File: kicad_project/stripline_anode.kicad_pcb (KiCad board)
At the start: 6 copper layers, 240 x 333.1 mm, 31 parts, among them J1 QRM8-078-05.0-L-D-A, U1 anode_pad, U10 anode_pad, U11 anode_pad, U12 anode_pad, U13 anode_pad, U14 anode_pad, U15 anode_pad, U16 anode_pad, U17 anode_pad, U18 anode_pad, U19 anode_pad, U2 anode_pad, U20 anode_pad, U21 anode_pad, U22 anode_pad, U23 anode_pad, U24 anode_pad, U25 anode_pad, U26 anode_pad, U27 anode_pad, U28 anode_pad, U29 anode_pad, U3 anode_pad, U30 anode_pad, U4 anode_pad, U5 anode_pad, U6 anode_pad, U7 anode_pad, U8 anode_pad, U9 anode_pad

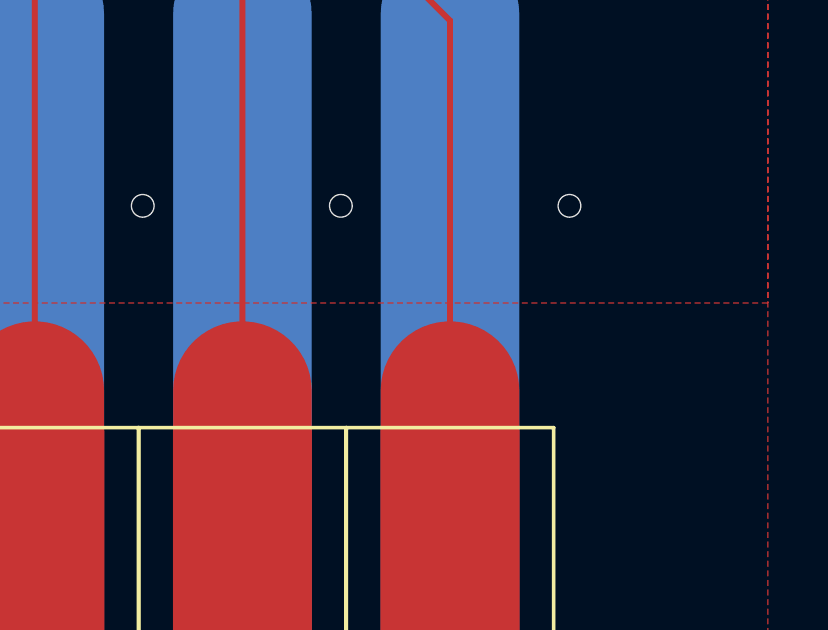
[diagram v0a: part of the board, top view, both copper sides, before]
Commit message: managed footprints into a proper pretty library
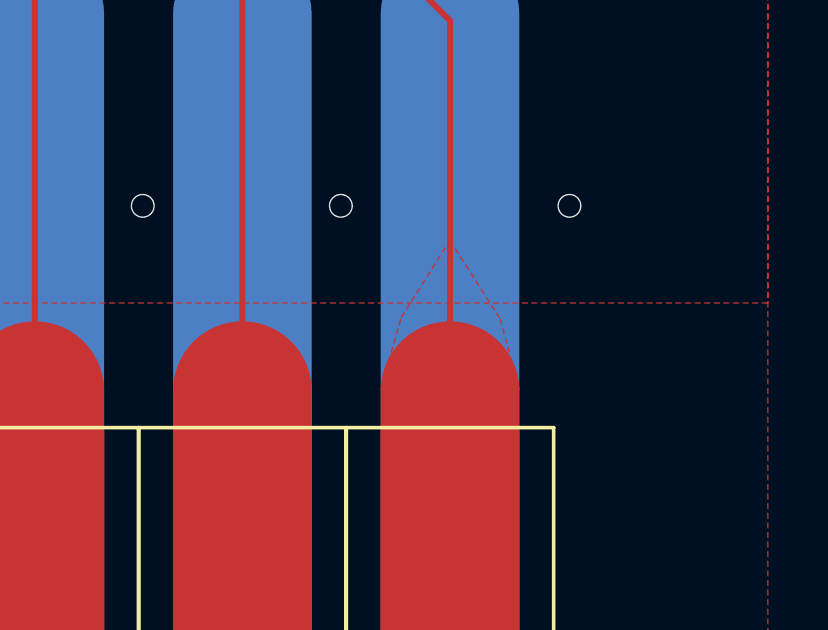
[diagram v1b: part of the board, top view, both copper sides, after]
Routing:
- added copper zone on F.Cu, net /c10
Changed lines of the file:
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@@
 (kicad_pcb (version 20211014) (generator pcbnew)
   (general
-    (thickness 1.5748)
+    (thickness 1.6)
   )
   (paper "C")
@@
   )
   (setup
+    (stackup
+      (layer "F.SilkS" (type "Top Silk Screen"))
+      (layer "F.Paste" (type "Top Solder Paste"))
+      (layer "F.Mask" (type "Top Solder Mask") (thickness 0.01))
+      (layer "F.Cu" (type "copper") (thickness 0.035))
+      (layer "dielectric 1" (type "core") (thickness 0.274) (material "FR4") (epsilon_r 4.5) (loss_tangent 0.02))
+      (layer "In1.Cu" (type "copper") (thickness 0.035))
+      (layer "dielectric 2" (type "prepreg") (thickness 0.274) (material "FR4") (epsilon_r 4.5) (loss_tangent 0.02))
+      (layer "In2.Cu" (type "copper") (thickness 0.035))
+      (layer "dielectric 3" (type "core") (thickness 0.274) (material "FR4") (epsilon_r 4.5) (loss_tangent 0.02))
+      (layer "In3.Cu" (type "copper") (thickness 0.035))
+      (layer "dielectric 4" (type "prepreg") (thickness 0.274) (material "FR4") (epsilon_r 4.5) (loss_tangent 0.02))
+      (layer "In4.Cu" (type "copper") (thickness 0.035))
+      (layer "dielectric 5" (type "core") (thickness 0.274) (material "FR4") (epsilon_r 4.5) (loss_tangent 0.02))
+      (layer "B.Cu" (type "copper") (thickness 0.035))
+      (layer "B.Mask" (type "Bottom Solder Mask") (thickness 0.01))
+      (layer "B.Paste" (type "Bottom Solder Paste"))
+      (layer "B.SilkS" (type "Bottom Silk Screen"))
+      (copper_finish "None")
+      (dielectric_constraints no)
+    )
     (pad_to_mask_clearance 0.051)
     (solder_mask_min_width 0.25)
@@
       )
     )
+  )
+  (zone (net 31) (net_name "/c10") (layer "F.Cu") (hatch edge 0.508)
+    (connect_pads (clearance 1.905))
+    (min_thickness 0.508)
+    (fill (thermal_gap 0.762) (thermal_bridge_width 0.762))
+    (polygon
+      (pts
+        (xy 376.3985 132.5155)
+        (xy 377.033177 134.870547)
+        (xy 372.413698 134.87034)
+        (xy 373.0985 132.4655)
+        (xy 374.7185 129.8955)
+      )
+    )

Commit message: Changed footprints to match new local footprint library. Redid edge cuts and user-drawings layer to have a well-positioning of ultem frame mounting holes. Put in four of those mounting holes, a few more to go. Put a rough edge-cuts layer (not positioned) so that copper pours work
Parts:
- added REF**: MountingHole_2.2mm_M2, MountingHole:MountingHole_2.2mm_M2, F.Cu at (389.4, 127.8)
- added REF**1: MountingHole_2.2mm_M2, MountingHole:MountingHole_2.2mm_M2, F.Cu at (159.4, 127.8)
- added REF**2: MountingHole_2.2mm_M2, MountingHole:MountingHole_2.2mm_M2, F.Cu at (389.4, 347.8)
- added REF**3: MountingHole_2.2mm_M2, MountingHole:MountingHole_2.2mm_M2, F.Cu at (159.4, 347.8)
- J1: footprint samtec:SAMTEC_QRM8-078-05.0-L-D-A -> stripline-anode-footprints:SAMTEC_QRM8-078-05.0-L-D-A
- U1, U10, U11, U12, U13, U14, U15, U16, U17, U18, U19, U20, U21, U22, U23, U24, U25, U26, U27, U28, U29, U3, U30, U4, U5, U6, U7, U8, U9: footprint AnodePads:stripline_30 -> stripline-anode-footprints:stripline_30
- U2: footprint AnodePads:stripline_30 -> LAPPD-readouts:stripline_30
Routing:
- net /b6: track 611.0 -> 276.0 mm
- net /c6: track 535.2 -> 316.2 mm
- net /c1: track 512.7 -> 293.8 mm
- net /b3: track 499.8 -> 280.9 mm
- net /b10: track 506.6 -> 287.7 mm
- net /a8: track 521.4 -> 302.5 mm
- net /c9: track 548.7 -> 329.8 mm
- net /c7: track 541.8 -> 322.9 mm
- net /c4: track 529.1 -> 310.2 mm
- net /c3: track 521.7 -> 302.8 mm
- net /c2: track 516.6 -> 297.7 mm
- net /c10: track 552.9 -> 334.0 mm
- net /b9: track 501.6 -> 282.7 mm
- net /b8: track 499.6 -> 280.6 mm
- net /b5: track 723.4 -> 504.5 mm
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- removed copper zone on F.Cu, net /c10
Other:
- board outline removed
- board text removed: "@Jacky, Evan, Henry Version 2 with Pad - GND - GND - GND - Trace "It works in Theory, now time for Practice.""
- board text removed: "SAMTEC cable connector"
- board text removed: "Square outer dimensions of Ultem frame"

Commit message: Various updates - Added pogo pin mounting board holes - Added additional Ultem frame mounting holes - Added "funnels" to ends of pickup striplines - Reduced size of loop around traces on back side of PCB
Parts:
- added ?: , , F.Cu at (159.3, 182.9)
- added ?: , , F.Cu at (274.4, 117.8)
- added ?: , , F.Cu at (274.4, 357.8)
- added ?: , , F.Cu at (232.9, 357.8)
- added ?: , , F.Cu at (295.1, 117.8)
- added ?: , , F.Cu at (336.6, 117.8)
- added ?: , , F.Cu at (295.1, 357.8)
- added ?: , , F.Cu at (253.6, 117.8)
- added ?: , , F.Cu at (315.9, 117.8)
- added ?: , , F.Cu at (232.9, 117.8)
- added ?: , , F.Cu at (159.3, 292.9)
- added ?: , , F.Cu at (315.8, 357.8)
- added ?: , , F.Cu at (336.5, 357.8)
- added ?: , , F.Cu at (253.6, 357.8)
- added ?: , , F.Cu at (389.4, 182.8)
- added ?: , , F.Cu at (389.4, 292.9)
- added ?: , , F.Cu at (212.2, 357.8)
- added ?: , , F.Cu at (212.2, 117.8)
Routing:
- net /b6: track 276.0 -> 394.5 mm, vias 2 -> 1
- net /b9: track 282.7 -> 401.1 mm, vias 2 -> 1
- net /b7: track 278.3 -> 396.7 mm, vias 2 -> 1
- net /b8: track 280.6 -> 398.9 mm, vias 2 -> 1
- net /a2: track 327.3 -> 445.6 mm, vias 2 -> 1
- net /a1: track 331.2 -> 449.4 mm, vias 2 -> 1
- net /a6: track 311.5 -> 429.7 mm, vias 2 -> 1
- net /a4: track 320.0 -> 438.1 mm, vias 2 -> 1
- net /a3: track 323.3 -> 441.3 mm, vias 2 -> 1
- net /b4: track 278.7 -> 396.7 mm, vias 2 -> 1
- net /b3: track 280.9 -> 398.9 mm, vias 2 -> 1
- net /b2: track 283.1 -> 401.1 mm, vias 2 -> 1
- net /b10: track 287.7 -> 405.6 mm, vias 2 -> 1
- net /b1: track 287.8 -> 405.6 mm, vias 2 -> 1
- net /a5: track 316.0 -> 433.6 mm, vias 2 -> 1
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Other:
- board outline added: 244.9 x 307 mm

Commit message: replaced narrow back traces with wide traces and corrected mechamical hole diameters
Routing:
- net /a1: track 449.4 -> 457.1 mm, vias 1 -> 2
- net /c5: track 425.6 -> 429.5 mm, vias 1 -> 2
- net /a7: track 421.8 -> 423.7 mm, vias 1 -> 2
- net /a3: track 441.3 -> 443.1 mm, vias 1 -> 2
- net /a2: track 445.6 -> 447.4 mm, vias 1 -> 2
- net /b4: vias 1 -> 2
- net /b3: vias 1 -> 2
- net /c2: track 411.7 -> 411.8 mm, vias 1 -> 2
- net /b8: vias 1 -> 2
- net /a8: vias 1 -> 2
- net /a9: track 410.4 -> 410.5 mm, vias 1 -> 2
- net /b7: vias 1 -> 2
- net /a10: vias 1 -> 2
- net /c7: vias 1 -> 2
- net /c1: vias 1 -> 2
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
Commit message: First draft layout of HV circuit. Things to refine: (1) ground return pads / mounting holes for gnd return. (2) Idea of how the high voltage inputs/outputs actually hook up to the LAPPD and incoming cables. (3) UL796 standard has 1.6kV/mm rating on distances between conductors. Is this tolerance actually OK, considering the present layout of gnd pour. (4) Do all of the components clear mechanical constraints of the LAPPD and Ultem frame, i.e. we wont have a solder mound where the detector or frame needs to be flush.
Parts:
- added C1: 0.1 uF, Capacitor_THT:C_Disc_D3.0mm_W1.6mm_P2.50mm, B.Cu at (383.7, 365.7)
- added C2: 0.1 uF, Capacitor_THT:C_Disc_D3.0mm_W1.6mm_P2.50mm, B.Cu at (165.3, 365.8)
- added C3: 100 pF, Capacitor_THT:CP_Radial_D8.0mm_P5.00mm, B.Cu at (177.9, 384.2)
- added C4: 10 nF, Capacitor_THT:CP_Radial_D8.0mm_P5.00mm, B.Cu at (190.8, 384.2)
- added C5: 100 pF, Capacitor_THT:CP_Radial_D8.0mm_P5.00mm, B.Cu at (165.7, 384.2)
- added C6: 10 nF, Capacitor_THT:CP_Radial_D8.0mm_P5.00mm, B.Cu at (231.7, 384.2)
- added C7: 10 nF, Capacitor_THT:CP_Radial_D8.0mm_P5.00mm, B.Cu at (285.8, 384.2)
- added C8: 10 nF, Capacitor_THT:CP_Radial_D8.0mm_P5.00mm, B.Cu at (340.8, 384.1)
- added D1: Zener 200V, Diode_THT:D_A-405_P12.70mm_Horizontal, B.Cu at (197.9, 422.3)
- added D2: Zener 200V, Diode_THT:D_A-405_P12.70mm_Horizontal, B.Cu at (277.7, 388.9)
- added D3: Zener 200V, Diode_THT:D_A-405_P12.70mm_Horizontal, B.Cu at (382.6, 376.8)
- added J10: sup_gnd_2, MountingHole:MountingHole_2.2mm_M2_Pad, F.Cu at (389.8, 411.3)
- added J2: SHV-cath-in, MountingHole:MountingHole_2.2mm_M2_Pad, B.Cu at (177.5, 422.3)
- added J3: SHV-mcps, MountingHole:MountingHole_2.2mm_M2_Pad, B.Cu at (205.2, 422.3)
- added J4: SHV-cath-out, MountingHole:MountingHole_2.2mm_M2_Pad, B.Cu at (160.6, 422.3)
- added J5: SHV-mcp1input, MountingHole:MountingHole_2.2mm_M2_Pad, B.Cu at (213.7, 422.3)
- added J6: SHV-mcp1output, MountingHole:MountingHole_2.2mm_M2_Pad, B.Cu at (234.0, 422.3)
- added J7: SHV-mcp2input, MountingHole:MountingHole_2.2mm_M2_Pad, B.Cu at (287.5, 422.3)
- added J8: SHV-mcp2output, MountingHole:MountingHole_2.2mm_M2_Pad, B.Cu at (343.4, 422.3)
- added J9: sup_gnd_1, MountingHole:MountingHole_2.2mm_M2_Pad, F.Cu at (157.3, 372.1)
- added POGO1: Conn_01x01, MountingHole:MountingHole_2.5mm_Pad, B.Cu at (253.9, 371.0)
- added POGO2: Conn_01x01, MountingHole:MountingHole_2.5mm_Pad, B.Cu at (212.2, 371.0)
- added POGO3: Conn_01x01, MountingHole:MountingHole_2.5mm_Pad, B.Cu at (336.4, 371.0)
- added POGO4: Conn_01x01, MountingHole:MountingHole_2.5mm_Pad, B.Cu at (295.1, 371.0)
- added R1: R, Resistor_THT:R_Axial_DIN0614_L14.3mm_D5.7mm_P20.32mm_Horizontal, B.Cu at (186.4, 408.8)
- added R10: R, Resistor_THT:R_Axial_DIN0614_L14.3mm_D5.7mm_P20.32mm_Horizontal, B.Cu at (295.1, 399.1)
- added R11: R, Resistor_THT:R_Axial_DIN0614_L14.3mm_D5.7mm_P20.32mm_Horizontal, B.Cu at (295.2, 409.0)
- added R12: R, Resistor_THT:R_Axial_DIN0614_L14.3mm_D5.7mm_P20.32mm_Horizontal, B.Cu at (320.5, 399.1)
- added R13: R, Resistor_THT:R_Axial_DIN0309_L9.0mm_D3.2mm_P12.70mm_Horizontal, B.Cu at (324.4, 409.0)
- added R14: R, Resistor_THT:R_Axial_DIN0614_L14.3mm_D5.7mm_P20.32mm_Horizontal, B.Cu at (363.1, 422.6)
- added R15: R, Resistor_THT:R_Axial_DIN0614_L14.3mm_D5.7mm_P20.32mm_Horizontal, B.Cu at (373.5, 422.7)
- added R16: R, Resistor_THT:R_Axial_DIN0614_L14.3mm_D5.7mm_P20.32mm_Horizontal, B.Cu at (363.3, 397.0)
- added R17: R, Resistor_THT:R_Axial_DIN0309_L9.0mm_D3.2mm_P12.70mm_Horizontal, B.Cu at (373.5, 389.5)
- added R2: R, Resistor_THT:R_Axial_DIN0614_L14.3mm_D5.7mm_P20.32mm_Horizontal, B.Cu at (186.2, 399.4)
- added R3: 100k, Resistor_THT:R_Axial_DIN0309_L9.0mm_D3.2mm_P12.70mm_Horizontal, B.Cu at (175.9, 411.3)
- added R4: R, Resistor_THT:R_Axial_DIN0614_L14.3mm_D5.7mm_P20.32mm_Horizontal, B.Cu at (211.7, 399.4)
- added R5: R, Resistor_THT:R_Axial_DIN0309_L9.0mm_D3.2mm_P12.70mm_Horizontal, B.Cu at (215.9, 408.9)
- added R6: R, Resistor_THT:R_Axial_DIN0614_L14.3mm_D5.7mm_P20.32mm_Horizontal, B.Cu at (260.7, 408.9)
- added R7: R, Resistor_THT:R_Axial_DIN0614_L14.3mm_D5.7mm_P20.32mm_Horizontal, B.Cu at (260.4, 399.4)
- added R8: R, Resistor_THT:R_Axial_DIN0614_L14.3mm_D5.7mm_P20.32mm_Horizontal, B.Cu at (265.6, 399.4)
- added R9: R, Resistor_THT:R_Axial_DIN0309_L9.0mm_D3.2mm_P12.70mm_Horizontal, B.Cu at (269.9, 408.8)
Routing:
- added copper zone on In4.Cu, net /High voltage distribution/supply-gnd
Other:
- board size 244.9 x 307 mm -> 244.9 x 363 mm

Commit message: A close to final version of high voltage circuitry, after having decided to go with SHV cable ends soldered on to SMD pads, potted, and strain relieved by zip ties. Also added SMA ports. This is one day before meeting to review
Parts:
- removed J10: sup_gnd_2, MountingHole:MountingHole_2.2mm_M2_Pad
- removed J2: SHV-cath-in, MountingHole:MountingHole_2.2mm_M2_Pad
- removed J3: SHV-mcps, MountingHole:MountingHole_2.2mm_M2_Pad
- removed J4: SHV-cath-out, MountingHole:MountingHole_2.2mm_M2_Pad
- removed J5: SHV-mcp1input, MountingHole:MountingHole_2.2mm_M2_Pad
- removed J6: SHV-mcp1output, MountingHole:MountingHole_2.2mm_M2_Pad
- removed J7: SHV-mcp2input, MountingHole:MountingHole_2.2mm_M2_Pad
- removed J8: SHV-mcp2output, MountingHole:MountingHole_2.2mm_M2_Pad
- removed J9: sup_gnd_1, MountingHole:MountingHole_2.2mm_M2_Pad
- added C10: 100 pF, Capacitor_SMD:C_1812_4532Metric_Pad1.57x3.40mm_HandSolder, B.Cu at (267.5, 383.1)
- added C11: 100 pF, Capacitor_SMD:C_1812_4532Metric_Pad1.57x3.40mm_HandSolder, B.Cu at (312.2, 383.1)
- added C12: 100 pF, Capacitor_SMD:C_1812_4532Metric_Pad1.57x3.40mm_HandSolder, B.Cu at (358.3, 383.1)
- added C9: 100 pF, Capacitor_SMD:C_1812_4532Metric_Pad1.57x3.40mm_HandSolder, B.Cu at (227.3, 384.8)
- added HV1: Conn_01x02, stripline-anode-footprints:SHV_cable_interface, B.Cu at (189.1, 415.9)
- added HV2: Conn_01x02, stripline-anode-footprints:SHV_cable_interface, B.Cu at (173.8, 415.9)
- added HV3: Conn_01x02, stripline-anode-footprints:SHV_cable_interface, B.Cu at (219.7, 415.9)
- added HV4: Conn_01x02, stripline-anode-footprints:SHV_cable_interface, B.Cu at (204.4, 415.9)
- added HV5: Conn_01x02, stripline-anode-footprints:SHV_cable_interface, B.Cu at (259.9, 415.9)
- added HV6: Conn_01x02, stripline-anode-footprints:SHV_cable_interface, B.Cu at (307.3, 415.9)
- added HV7: Conn_01x02, stripline-anode-footprints:SHV_cable_interface, B.Cu at (350.9, 415.9)
- added R18: 200, Resistor_SMD:R_2512_6332Metric_Pad1.40x3.35mm_HandSolder, B.Cu at (375.9, 368.9)
- added R19: 200, Resistor_SMD:R_2512_6332Metric_Pad1.40x3.35mm_HandSolder, B.Cu at (173.7, 368.3)
- added SM1: Conn_Coaxial, Connector_Coaxial:SMA_Johnson_142-0711-271, F.Cu at (183.7, 106.2)
- added SM2: Conn_Coaxial, Connector_Coaxial:SMA_Johnson_142-0711-271, B.Cu at (174.1, 113.9)
- added SM3: Conn_Coaxial, Connector_Coaxial:SMA_Johnson_142-0711-271, B.Cu at (374.7, 113.9)
- added SM4: Conn_Coaxial, Connector_Coaxial:SMA_Johnson_142-0711-271, B.Cu at (320.8, 363.4)
- added SM5: Conn_Coaxial, Connector_Coaxial:SMA_Johnson_142-0711-271, B.Cu at (331.8, 363.4)
- added SM6: Conn_Coaxial, Connector_Coaxial:SMA_Johnson_142-0711-271, B.Cu at (342.7, 363.4)
- C1, C2: footprint Capacitor_THT:C_Disc_D3.0mm_W1.6mm_P2.50mm -> Capacitor_SMD:C_1812_4532Metric_Pad1.57x3.40mm_HandSolder
- C3, C5: footprint Capacitor_THT:CP_Radial_D8.0mm_P5.00mm -> Capacitor_SMD:C_1812_4532Metric_Pad1.57x3.40mm_HandSolder
- C4, C6, C7, C8: footprint Capacitor_THT:CP_Radial_D8.0mm_P5.00mm -> Capacitor_SMD:C_2220_5650Metric_Pad1.97x5.40mm_HandSolder
- D1, D2, D3: footprint Diode_THT:D_A-405_P12.70mm_Horizontal -> Diode_SMD:D_SOD-123
- R1, R10, R11, R12, R14, R15, R16, R2, R4, R6, R7, R8: footprint Resistor_THT:R_Axial_DIN0614_L14.3mm_D5.7mm_P20.32mm_Horizontal -> Resistor_SMD:R_2512_6332Metric_Pad1.40x3.35mm_HandSolder
- R13, R17, R3, R5, R9: footprint Resistor_THT:R_Axial_DIN0309_L9.0mm_D3.2mm_P12.70mm_Horizontal -> Resistor_SMD:R_2512_6332Metric_Pad1.40x3.35mm_HandSolder
- moved R1 53.0 mm to (237.6, 395.4)
- moved R2 52.2 mm to (237.6, 390.0)
- moved D3 37.2 mm to (345.9, 383.1)
- moved R4 36.6 mm to (247.1, 390.1)
- moved R5 33.9 mm to (247.0, 395.4)
- moved R11 33.9 mm to (326.0, 394.9)
- moved D1 33.4 mm to (196.6, 388.9)
- moved R14 33.2 mm to (365.6, 389.5), turned to 0 degrees
- moved R10 32.3 mm to (326.0, 389.7)
- moved C4 29.9 mm to (220.7, 384.8)
- moved C6 29.1 mm to (260.8, 383.1)
- moved R15 29.0 mm to (365.6, 394.8), turned to 0 degrees
- moved R8 24.2 mm to (287.7, 389.7)
- moved R3 23.7 mm to (181.6, 388.3)
- moved R6 22.6 mm to (278.5, 395.1), turned to 0 degrees
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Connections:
- net Net-(C3-Pad2) renamed /High voltage distribution/cath-in
- net Net-(C5-Pad2) renamed /High voltage distribution/cath_out
- C1 pad 1: /High voltage distribution/supply-gnd -> Net-(C1-Pad1)
- C2 pad 1: /High voltage distribution/supply-gnd -> Net-(C2-Pad1)
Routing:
- net /High voltage distribution/mcp2input: track 0.00 -> 21.8 mm, vias 0 -> 27
- net /a1: track 457.1 -> 470.9 mm
- net /c4: track 421.8 -> 431.0 mm
- net /c3: track 416.7 -> 425.7 mm
- net /c10: track 449.4 -> 457.3 mm
- net /c5: track 429.5 -> 437.3 mm
- net Net-(R1-Pad2): track 0.00 -> 6.67 mm
- net Net-(R14-Pad2): track 0.00 -> 6.48 mm
- net Net-(R10-Pad2): track 0.00 -> 6.42 mm
- net Net-(R6-Pad2): track 0.00 -> 6.32 mm
- net Net-(C2-Pad1): track 0.00 -> 5.44 mm
- net Net-(C1-Pad1): track 0.00 -> 5.08 mm
- net /High voltage distribution/supply-gnd: vias 0 -> 58
- net /High voltage distribution/mcp2output: vias 0 -> 29
- net /High voltage distribution/mcp1output: vias 0 -> 29
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- added copper zone on In3.Cu, net /High voltage distribution/cath-in
- added copper zone on In3.Cu, net /High voltage distribution/cath_out
- added copper zone on In3.Cu, net /High voltage distribution/mcp1input
- added copper zone on In3.Cu, net /High voltage distribution/mcp1output
- added copper zone on In3.Cu, net /High voltage distribution/mcp2input
- added copper zone on In3.Cu, net /High voltage distribution/mcp2output
- added copper zone on F.Cu, net /High voltage distribution/supply-gnd
- removed copper zone on In4.Cu, net /High voltage distribution/supply-gnd
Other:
- board size 244.9 x 363 mm -> 244.9 x 347.7 mm

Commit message: Made adjustments to all via aspect ratios to fit basic standards of PCB way and a 5mm board. Moved some of the copper pours on the HV circuit side. About to dive into adjusting gnd stitching and gnd pattern
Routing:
- net /GND: track 473.9 -> 504.4 mm, vias 229 -> 225
- net Net-(R14-Pad2): track 6.48 -> 11.9 mm
- net Net-(R6-Pad2): track 6.32 -> 11.7 mm
- net Net-(R1-Pad2): track 6.67 -> 12.0 mm
- net Net-(R10-Pad2): track 6.42 -> 11.7 mm
- net /High voltage distribution/supply-gnd: vias 58 -> 33
- net /High voltage distribution/mcp2output: vias 29 -> 0
- net /High voltage distribution/mcp2input: vias 27 -> 0
- net /High voltage distribution/mcp1output: vias 29 -> 0
- net /High voltage distribution/mcp1input: vias 24 -> 0
- net /High voltage distribution/cath_out: vias 11 -> 0
- net /High voltage distribution/cath-in: vias 13 -> 0
- added copper zone on B.Cu, net /High voltage distribution/cath-in
- added copper zone on B.Cu, net /High voltage distribution/cath_out
- added copper zone on B.Cu, net /High voltage distribution/mcp1input
- added copper zone on B.Cu, net /High voltage distribution/mcp1output
- added copper zone on B.Cu, net /High voltage distribution/mcp2input
- added copper zone on B.Cu, net /High voltage distribution/mcp2output
- removed copper zone on In3.Cu, net /High voltage distribution/cath-in
- removed copper zone on In3.Cu, net /High voltage distribution/cath_out
- removed copper zone on In3.Cu, net /High voltage distribution/mcp1input
- removed copper zone on In3.Cu, net /High voltage distribution/mcp1output
- removed copper zone on In3.Cu, net /High voltage distribution/mcp2input
- removed copper zone on In3.Cu, net /High voltage distribution/mcp2output

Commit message: Board design is ready for production.
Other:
- board text added: "Cathode input"
- board text added: "Cathode output (to LAPPD)"
- board text added: "Gap between MCPs"
- board text added: "MCP1 Input"
- board text added: "MCP1 Output"
- board text added: "MCP2 Input"
- board text added: "MCP2 Output"
- board text added: "Parallel with MCP resist."
- board text added: "Supply Gnd"
